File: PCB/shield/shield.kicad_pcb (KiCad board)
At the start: 2 copper layers, 81.2 x 87.2 mm, 16 parts, among them J1 QTR-8A, J13 Motor, J3 Servo, J4 Battery, J5 Joystick, J6 OLED, Q1 SI2301DS, SW1 SW_SPST, U1 LM2596, U2 ESP32-S3-DevKitC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

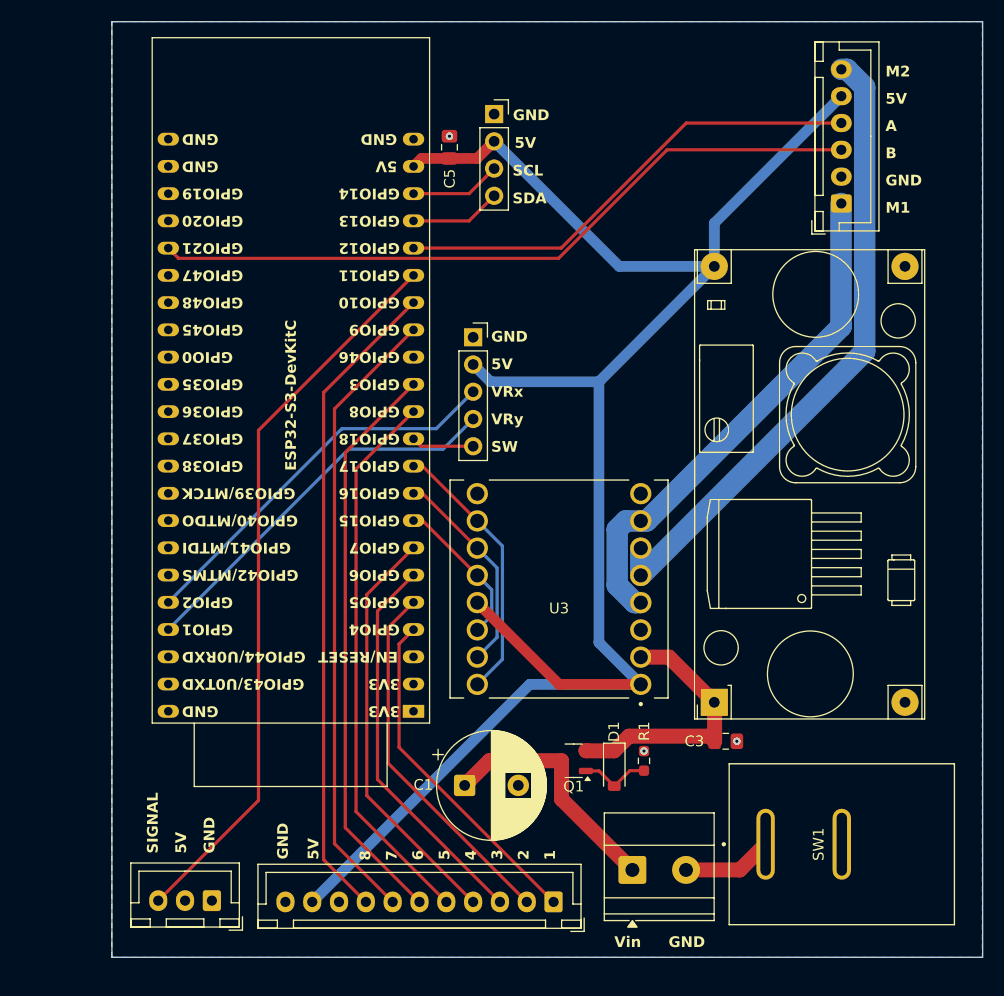
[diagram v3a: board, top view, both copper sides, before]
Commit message: feat: change pcb design, make pcb smaller by removing joystick and screen
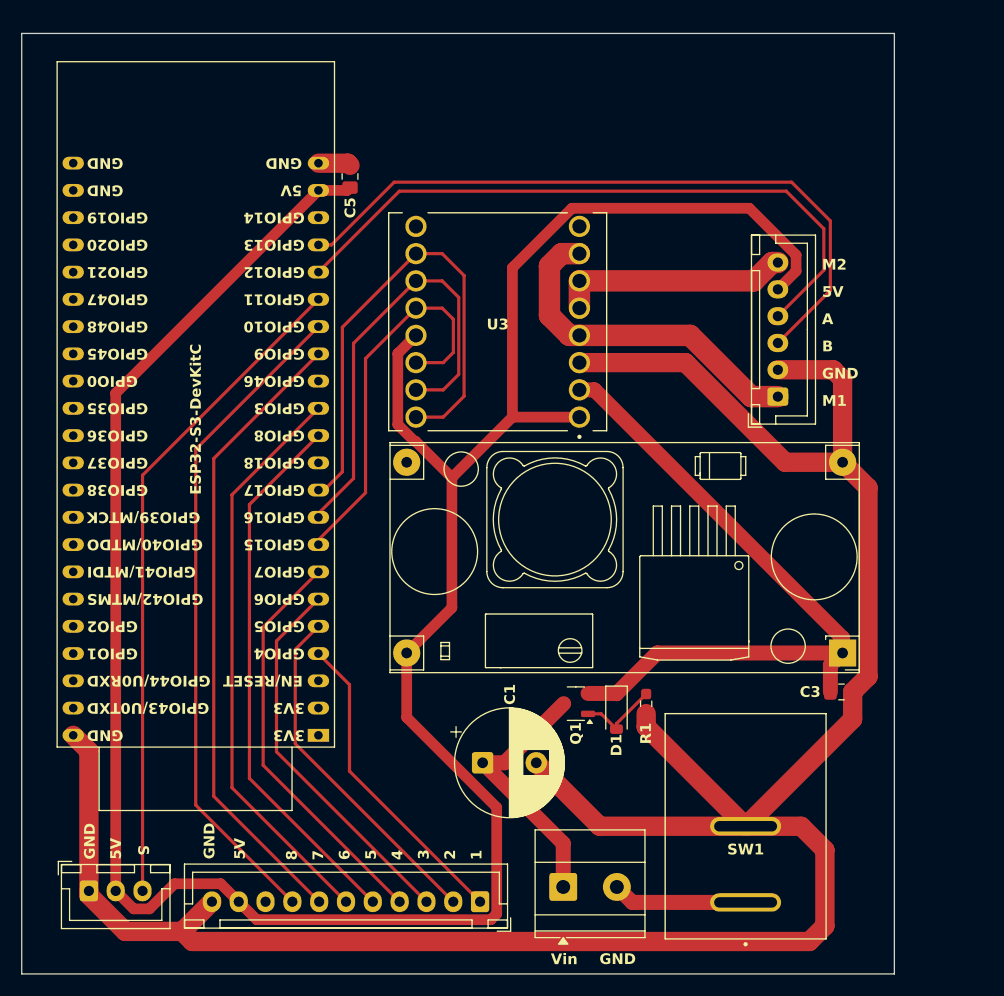
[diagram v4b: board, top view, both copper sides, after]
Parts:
- removed J5: Joystick, Connector_PinSocket_2.54mm:PinSocket_1x05_P2.54mm_Vertical
- removed J6: OLED, Connector_PinSocket_2.54mm:PinSocket_1x04_P2.54mm_Vertical
- moved U3 25.6 mm to (68.6, 95.3)
- moved J13 19.0 mm to (94.7, 102.3)
- moved U1 12.8 mm to (100.7, 126.2), turned to 180 degrees
- moved C3 11.7 mm to (100.6, 129.8)
- moved J3 11.5 mm to (30.4, 148.3), turned to 0 degrees
- moved C5 9.66 mm to (54.8, 81.7)
- moved U2 9.14 mm to (51.8, 133.8)
- moved SW1 9.12 mm to (91.7, 142.3), turned to 90 degrees
- moved J1 6.85 mm to (66.9, 149.4)
- moved J4 6.64 mm to (74.7, 148.0)
- moved D1 5.33 mm to (79.6, 131.6)
- moved Q1 5.33 mm to (75.8, 130.9)
- moved R1 5.33 mm to (82.4, 130.9), turned to -90 degrees
- moved C1 2.69 mm to (67.2, 136.4)
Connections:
- J13 pad 3: /GPIO21 -> /GPIO13
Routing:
- net GND: track 0.00 -> 227.3 mm, vias 3 -> 0
- net +5V: track 169.5 -> 239.6 mm
- net /GPIO21: track 67.3 -> 0.00 mm
- net /GPIO13: track 8.49 -> 65.1 mm
- net VCC: track 25.0 -> 64.9 mm
- net /M2: track 59.6 -> 21.7 mm
- net /GPIO2: track 36.6 -> 0.00 mm
- net /GPIO1: track 36.6 -> 0.00 mm
- net /GPIO17: track 25.2 -> 48.0 mm
- net /GPIO15: track 14.3 -> 36.7 mm
- net /GPIO16: track 19.8 -> 42.2 mm
- net /GPIO12: track 44.7 -> 61.6 mm
- net /M1: track 48.3 -> 32.3 mm
- net /GPIO14: track 8.48 -> 0.00 mm
- net /GPIO11: track 68.1 -> 61.9 mm
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- removed copper zone on B.Cu, net GND
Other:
- board size 81.2 x 87.2 mm -> 81.4 x 87.7 mm
- board text added: "S"
- board text removed: "SCL"
- board text removed: "SDA"
- board text removed: "SIGNAL"
- board text removed: "SW"
- board text removed: "VRx"
- board text removed: "VRy"

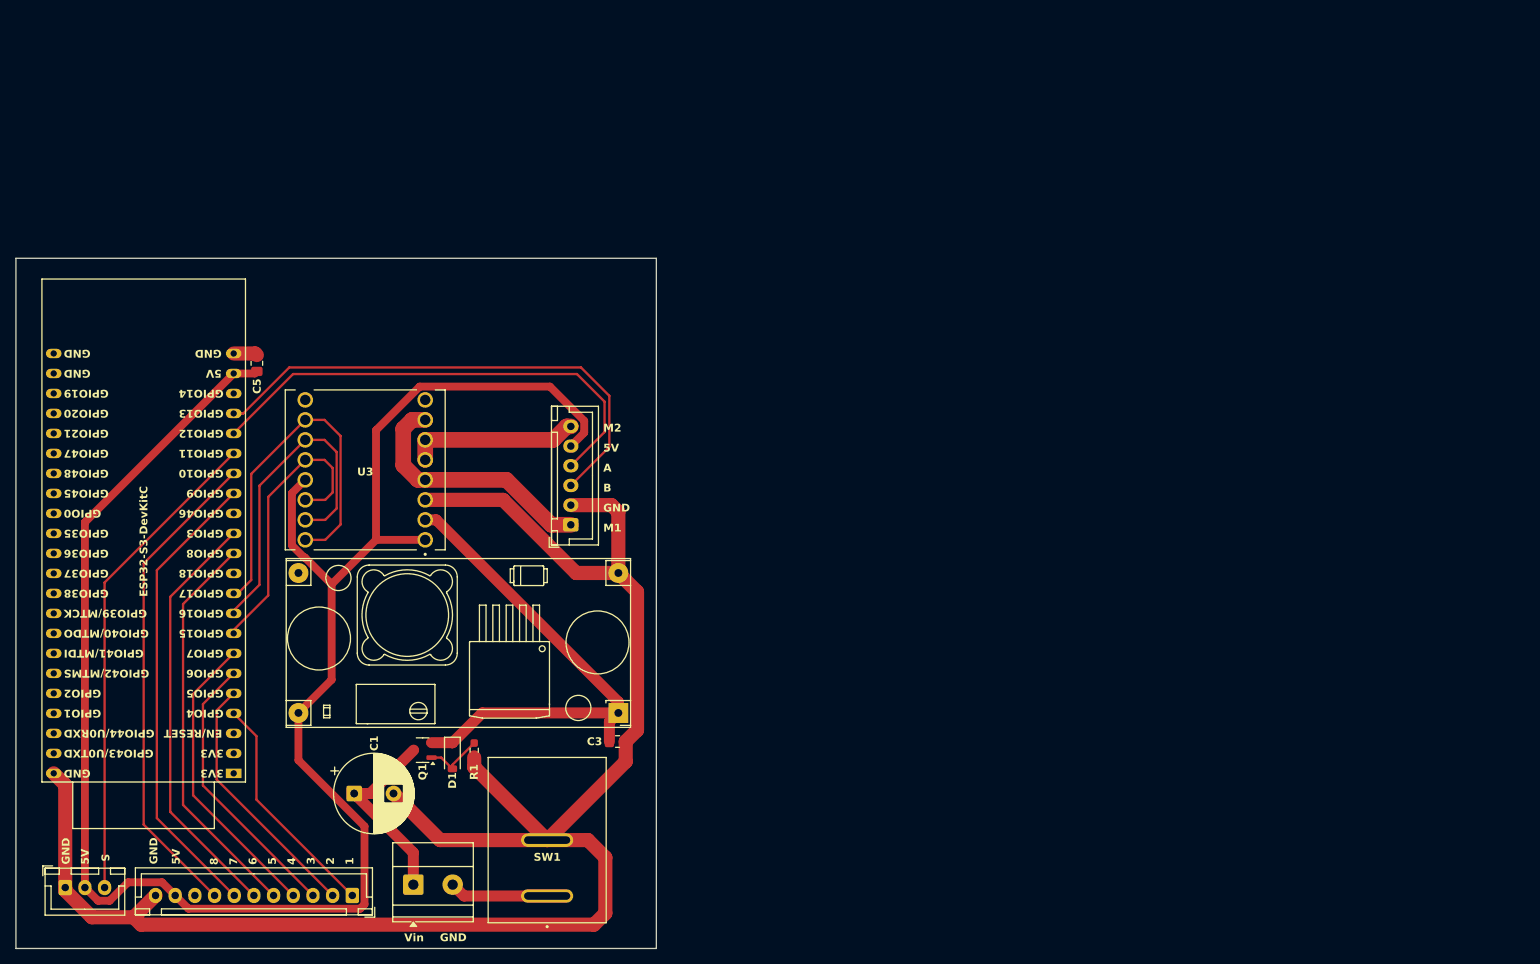
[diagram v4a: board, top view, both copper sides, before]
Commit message: feat: change LM2596S to MP1584EN; change to 2-layer pcb
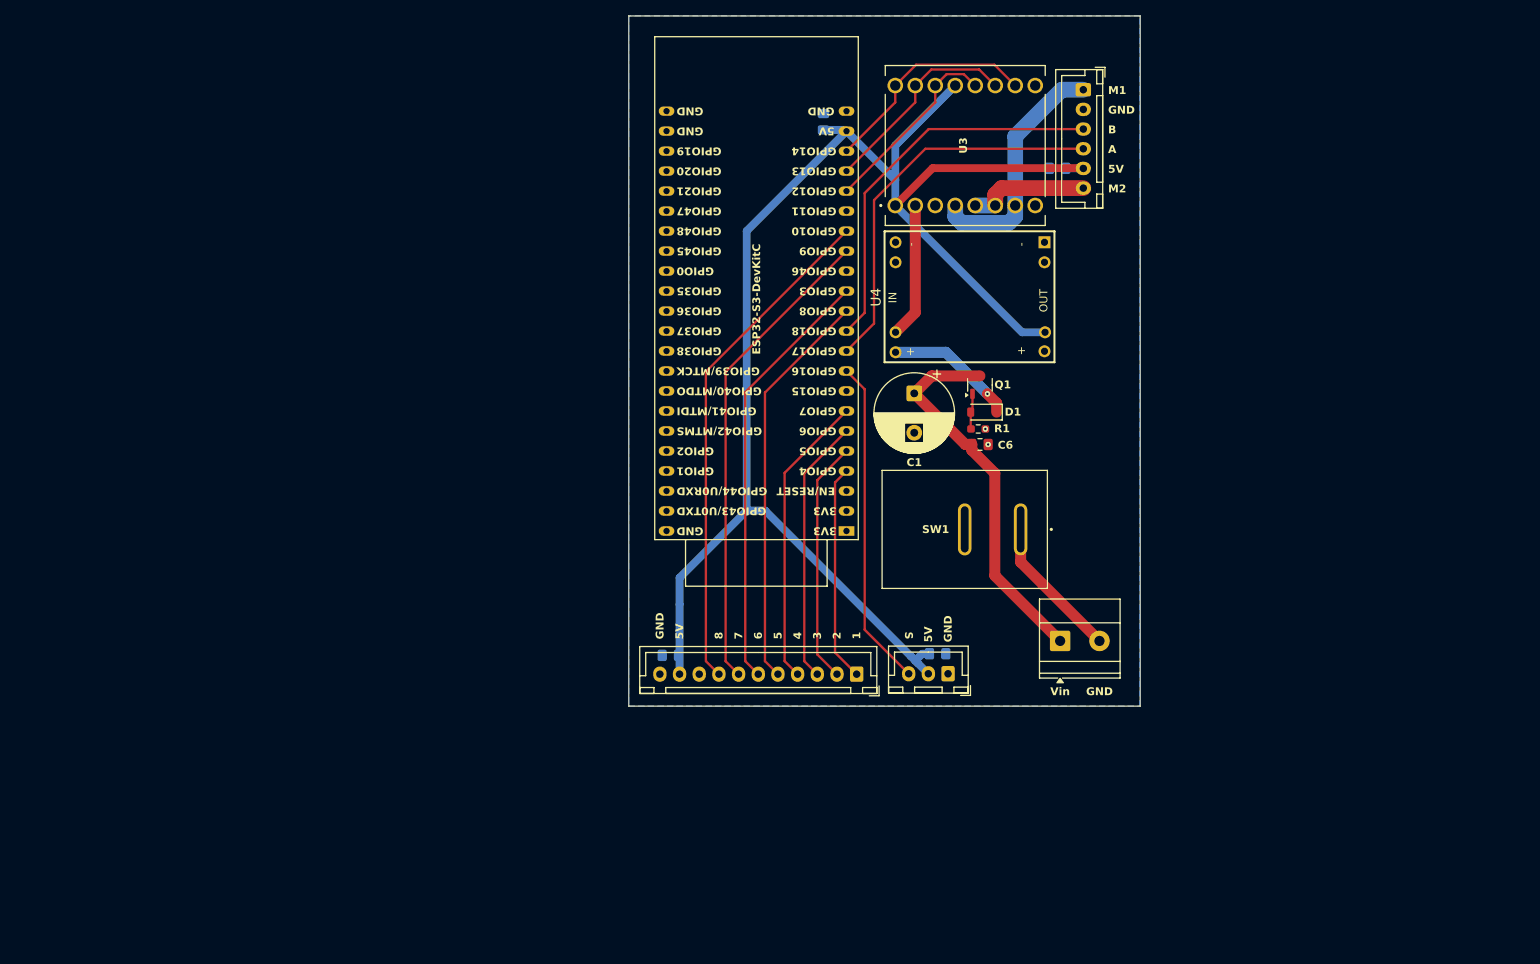
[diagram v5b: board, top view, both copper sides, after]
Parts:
- removed C3: 0.1uF, Capacitor_SMD:C_0805_2012Metric_Pad1.18x1.45mm_HandSolder
- removed U1: LM2596, KiCad:YAAJ_DCDC_StepDown_LM2596
- added C2: 0.1uF, Capacitor_SMD:C_0805_2012Metric_Pad1.18x1.45mm_HandSolder, B.Cu at (107.3, 118.8)
- added C4: 0.1uF, Capacitor_SMD:C_0805_2012Metric_Pad1.18x1.45mm_HandSolder, B.Cu at (141.3, 118.6)
- added C6: 0.1uF, Capacitor_SMD:C_0805_2012Metric_Pad1.18x1.45mm_HandSolder, F.Cu at (146.7, 92.1)
- added C7: 0.1uF, Capacitor_SMD:C_0805_2012Metric_Pad1.18x1.45mm_HandSolder, B.Cu at (156.5, 57.0)
- added U4: MP1584EN, MP1584EN:MP1584EN, F.Cu at (134.5, 81.6)
- C5: moved to B.Cu
- SW1: footprint Rocket Switch:SW_RF1-1A-DC-2-R-1 -> RF1-1A-DC-2-R-1:SW_RF1-1A-DC-2-R-1
- moved J3 115.4 mm to (142.6, 121.2), turned to 180 degrees
- moved J4 87.8 mm to (156.8, 117.0)
- moved C1 87.4 mm to (138.3, 85.6), turned to -90 degrees
- moved U3 86.7 mm to (144.8, 54.1), turned to 90 degrees
- moved J13 85.4 mm to (159.8, 47.0), turned to -90 degrees
- moved Q1 84.7 mm to (146.6, 84.5), turned to 90 degrees
- moved U2 83.7 mm to (129.7, 103.0)
- moved D1 80.4 mm to (147.1, 87.9), turned to 180 degrees
- moved C5 78.3 mm to (126.8, 51.1)
- moved R1 75.9 mm to (146.4, 90.1), turned to 0 degrees
- moved J1 70.0 mm to (131.0, 121.2)
- moved SW1 66.1 mm to (144.7, 102.8), turned to 180 degrees
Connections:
- J13 pad 3: /GPIO13 -> /GPIO18
- J13 pad 4: /GPIO12 -> /GPIO17
- J3 pad 3: /GPIO11 -> /GPIO16
- U3 pad 10: /GPIO17 -> /GPIO14
- U3 pad 11: /GPIO16 -> /GPIO13
- U3 pad 12: /GPIO15 -> /GPIO12
- U3 pad 14: /GPIO15 -> /GPIO12
- U3 pad 15: /GPIO16 -> /GPIO13
- U3 pad 16: /GPIO17 -> /GPIO14
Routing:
- net GND: track 227.3 -> 0.00 mm, vias 0 -> 2
- net /GPIO11: track 61.9 -> 0.00 mm
- net /GPIO18: track 0.00 -> 49.6 mm
- net +5V: track 239.6 -> 195.8 mm
- net /GPIO13: track 65.1 -> 26.3 mm
- net /GPIO12: track 61.6 -> 24.4 mm
- net /GPIO15: track 36.7 -> 0.00 mm
- net VCC: track 64.9 -> 33.8 mm, vias 0 -> 1
- net /GPIO14: track 0.00 -> 28.3 mm
- net Net-(J4-Pin_1): track 24.5 -> 48.9 mm
- net /M2: track 21.7 -> 15.5 mm
- net Net-(J4-Pin_2): track 12.6 -> 18.3 mm
- net Net-(D1-A): track 7.66 -> 4.57 mm
- net /GPIO10: track 62.1 -> 64.4 mm
- net /GPIO17: track 48.0 -> 49.9 mm
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- added copper zone on B.Cu, net GND
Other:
- board size 81.4 x 87.7 mm -> 65 x 87.7 mm
- board text removed: "1"
- board text removed: "2"
- board text removed: "3"
- board text removed: "4"
- board text removed: "5"
- board text removed: "5V"
- board text removed: "6"
- board text removed: "7"
- board text removed: "8"
- board text removed: "A"
- board text removed: "B"
- board text removed: "GND"
- board text removed: "M1"
- board text removed: "M2"
- board text removed: "S"
- board text removed: "Vin"

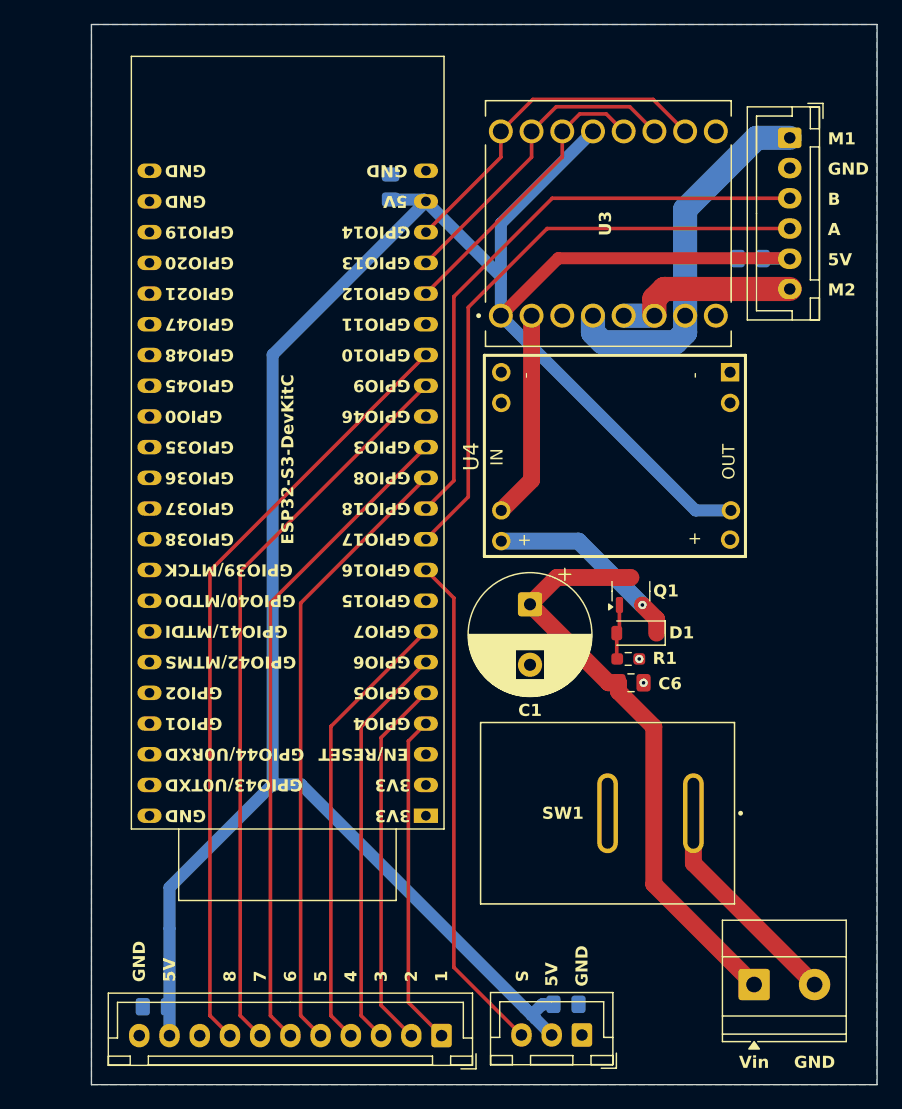
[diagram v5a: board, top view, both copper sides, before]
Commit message: feat: change esp32 footprint using altium-based lib
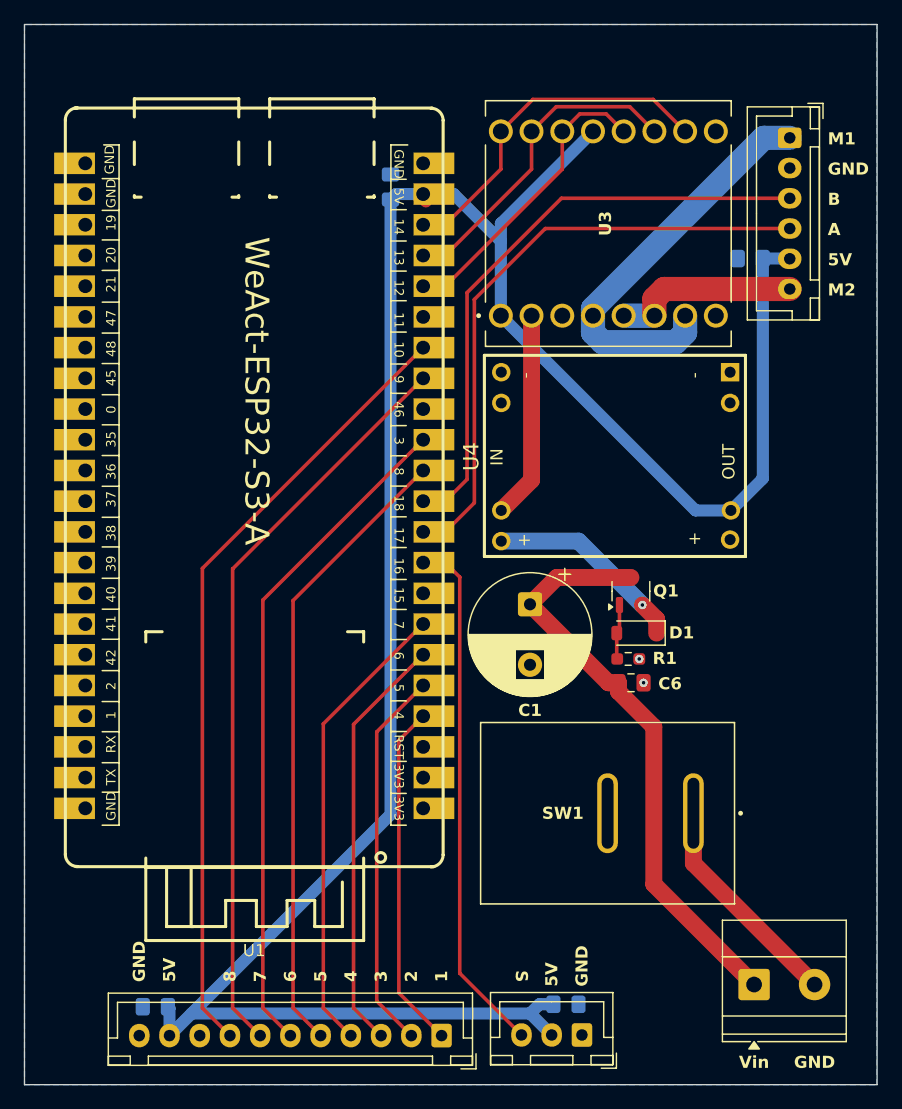
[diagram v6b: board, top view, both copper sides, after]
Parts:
- removed U2: ESP32-S3-DevKitC, PCM_Espressif:ESP32-S3-DevKitC
- added U1: WeAct-ESP32-S3-A, WeAct-ESP32-S3-A:WeAct-ESP32-S3-A, F.Cu at (115.9, 72.8)
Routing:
- net +5V: track 195.8 -> 191.3 mm
- net /M1: track 31.0 -> 33.8 mm
- net /GPIO16: track 41.7 -> 43.5 mm
- net /GPIO4: track 27.5 -> 28.7 mm
- net /GPIO3: track 54.7 -> 55.7 mm
- net /GPIO10: track 64.4 -> 65.4 mm
- net /GPIO8: track 51.1 -> 52.1 mm
- net /GPIO7: track 37.4 -> 38.4 mm
- net /GPIO6: track 33.8 -> 34.8 mm
- net /GPIO9: track 60.8 -> 61.8 mm
- net /GPIO5: track 30.9 -> 31.7 mm
- net /GPIO17: track 49.9 -> 50.6 mm
- net /GPIO13: track 26.3 -> 26.9 mm
- net /GPIO12: track 24.4 -> 24.9 mm
- net /GPIO14: track 28.3 -> 28.9 mm
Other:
- board size 65 x 87.7 mm -> 70.5 x 87.7 mm
